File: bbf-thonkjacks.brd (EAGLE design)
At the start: 20.3 x 52.1 mm, 7 parts, among them J1 WQP-PJ301M-12_JACK, J2 WQP-PJ301M-12_JACK, J3 WQP-PJ301M-12_JACK, J4 WQP-PJ301M-12_JACK

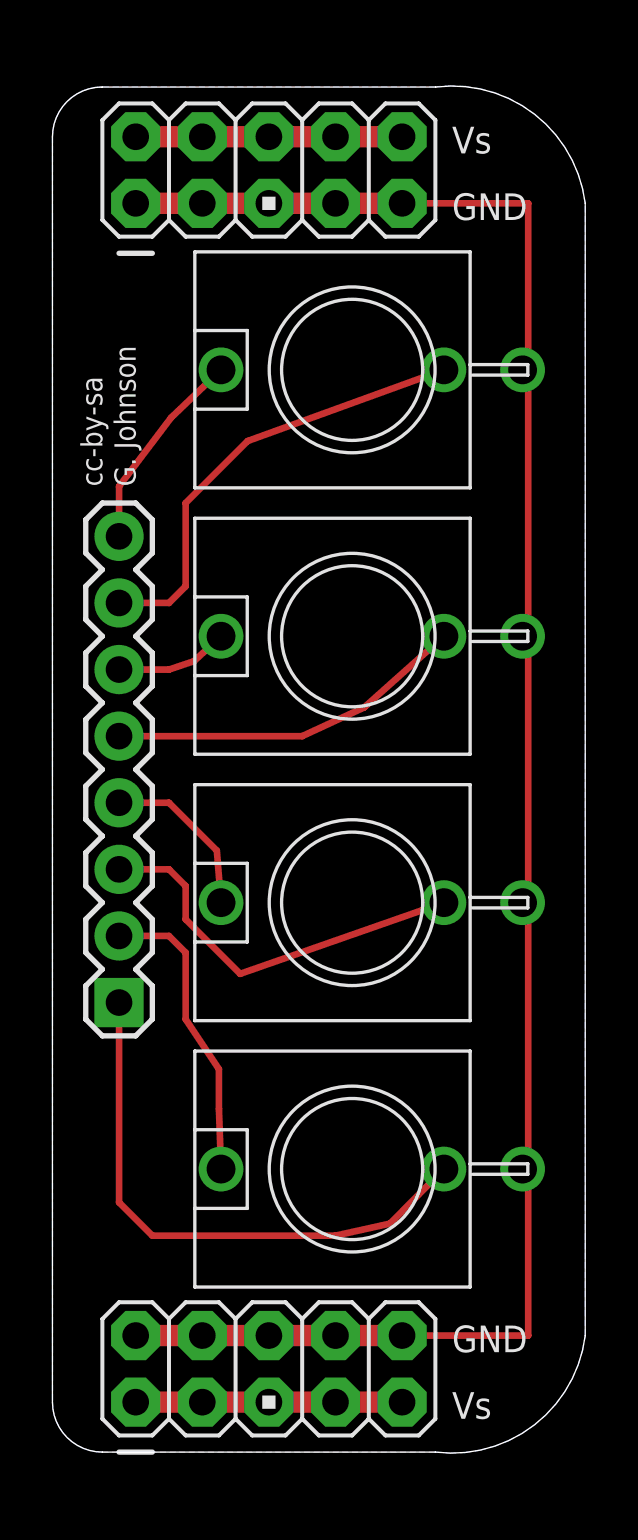
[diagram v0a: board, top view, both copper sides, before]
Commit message: thonkiconn jacks wider
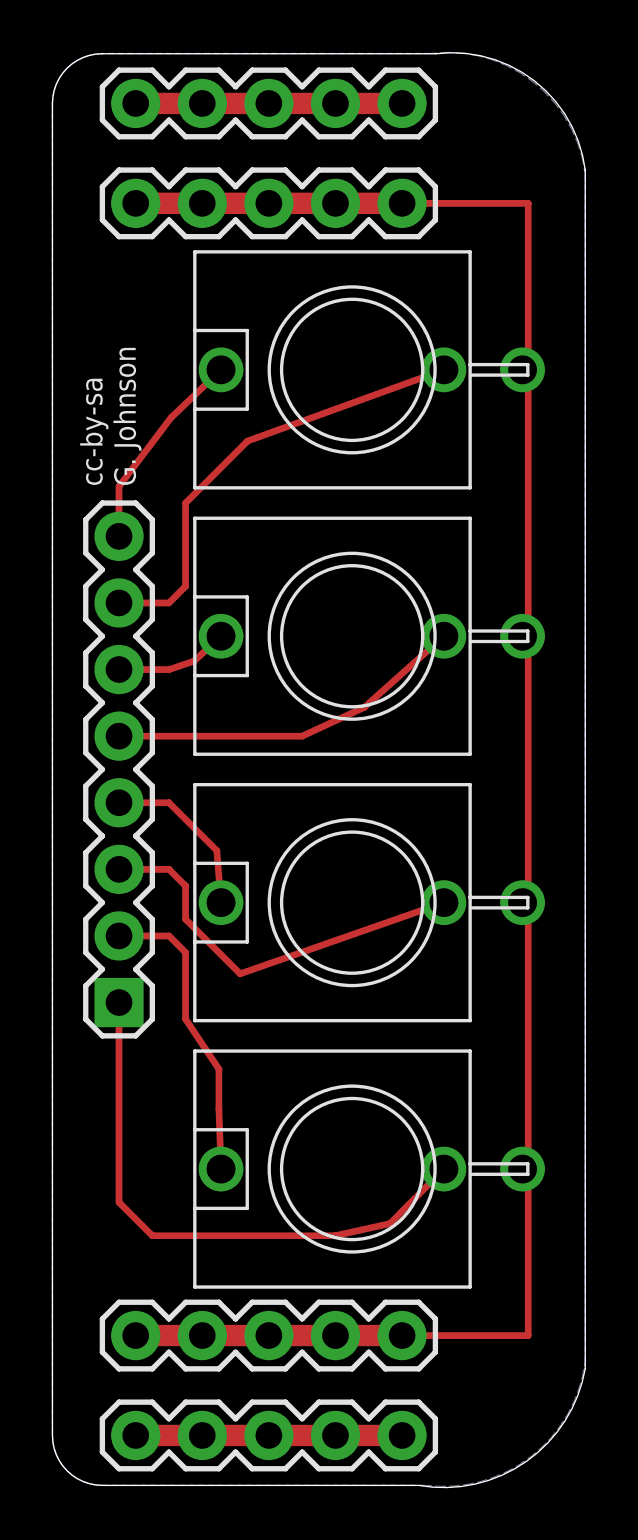
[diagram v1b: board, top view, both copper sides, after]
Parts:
- removed JP1, JP3: M05X2PTH, SparkFun:AVR_ICSP
- added JP4, JP5, JP6, JP7: (no value), SparkFun:1X05
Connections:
- net GND: now also JP4.1, JP4.2, JP4.3, JP4.4, JP4.5, JP6.1, JP6.2, JP6.3, JP6.4, JP6.5; no longer JP1.1, JP1.3, JP1.5, JP1.7, JP1.9, JP3.10, JP3.2, JP3.4, JP3.6, JP3.8
- net VCC: now also JP5.1, JP5.2, JP5.3, JP5.4, JP5.5; no longer JP1.10, JP1.2, JP1.4, JP1.6, JP1.8
- net VEE: now also JP7.1, JP7.2, JP7.3, JP7.4, JP7.5; no longer JP3.1, JP3.3, JP3.5, JP3.7, JP3.9
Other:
- board size 20.3 x 52.1 mm -> 20.3 x 54.7 mm
- board text removed: "GND"
- board text removed: "Vs"
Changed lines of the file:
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@@
 <?xml version="1.0" encoding="utf-8"?>
 <!DOCTYPE eagle SYSTEM "eagle.dtd">
-<eagle version="7.3.0">
+<eagle version="9.6.2">
 <drawing>
 <settings>
-<setting alwaysvectorfont="yes"/>
+<setting alwaysvectorfont="no"/>
+<setting keepoldvectorfont="yes"/>
 <setting verticaltext="up"/>
 </settings>
-<grid distance="25" unitdist="mil" unit="mm" style="lines" multiple="2" display="yes" altdistance="1" altunitdist="mm" altunit="mm"/>
+<grid distance="25" unitdist="mil" unit="inch" style="lines" multiple="1" display="yes" altdistance="0.025" altunitdist="inch" altunit="inch"/>
 <layers>
 <layer number="1" name="Top" color="4" fill="1" visible="yes" active="yes"/>
@@
 <board>
 <plain>
-<wire x1="14.605" y1="0" x2="20.32" y2="4.445" width="0" layer="20" curve="90"/>
-<wire x1="20.32" y1="4.445" x2="20.32" y2="47.625" width="0" layer="20"/>
-<wire x1="20.32" y1="47.625" x2="14.615" y2="52.06" width="0" layer="20" curve="90"/>
-<wire x1="14.615" y1="52.06" x2="1.895" y2="52.06" width="0" layer="20"/>
-<wire x1="1.895" y1="52.06" x2="0" y2="50.165" width="0" layer="20" curve="90"/>
-<wire x1="0" y1="50.165" x2="0" y2="1.905" width="0" layer="20"/>
-<wire x1="0" y1="1.905" x2="1.905" y2="0" width="0" layer="20" curve="90"/>
-<wire x1="1.905" y1="0" x2="14.605" y2="0" width="0" layer="20"/>
+<wire x1="13.97" y1="-1.27" x2="20.32" y2="3.175" width="0" layer="20" curve="90"/>
+<wire x1="20.32" y1="3.175" x2="20.32" y2="48.895" width="0" layer="20"/>
+<wire x1="20.32" y1="48.895" x2="14.615" y2="53.33" width="0" layer="20" curve="90"/>
+<wire x1="14.615" y1="53.33" x2="1.895" y2="53.33" width="0" layer="20"/>
+<wire x1="1.895" y1="53.33" x2="0" y2="51.435" width="0" layer="20" curve="90"/>
+<wire x1="0" y1="51.435" x2="0" y2="0.635" width="0" layer="20"/>
+<wire x1="0" y1="0.635" x2="1.905" y2="-1.27" width="0" layer="20" curve="90"/>
+<wire x1="1.905" y1="-1.27" x2="13.97" y2="-1.27" width="0" layer="20"/>
 <text x="1.905" y="36.83" size="0.8128" layer="25" ratio="15" rot="R90">cc-by-sa</text>
 <text x="3.175" y="36.83" size="0.8128" layer="25" ratio="15" rot="R90">G. Johnson</text>
-<text x="15.24" y="46.99" size="1.016" layer="21" font="vector">GND</text>
-<text x="15.24" y="3.81" size="1.016" layer="21" font="vector">GND</text>
-<text x="15.24" y="1.27" size="1.016" layer="21" font="vector">Vs</text>
-<text x="15.24" y="49.53" size="1.016" layer="21" font="vector">Vs</text>
 </plain>
 <attributes>
@@
 <param name="dpMaxLengthDifference" value="10mm"/>
 <param name="dpGapFactor" value="2.5"/>
-<param name="checkGrid" value="0"/>
 <param name="checkAngle" value="1"/>
 <param name="checkFont" value="1"/>
 <param name="checkRestrict" value="1"/>
+<param name="checkStop" value="0"/>
+<param name="checkValues" value="0"/>
+<param name="checkNames" value="1"/>
+<param name="checkWireStubs" value="1"/>
+<param name="checkPolygonWidth" value="0"/>
 <param name="useDiameter" value="13"/>
 <param name="maxErrors" value="50"/>
@@
 </autorouter>
 <elements>
-<element name="JP1" library="SparkFun" package="AVR_ICSP" value="M05X2PTH" x="8.255" y="48.895" smashed="yes" rot="R90"/>
-<element name="JP3" library="SparkFun" package="AVR_ICSP" value="M05X2PTH" x="8.255" y="3.175" smashed="yes" rot="R90"/>
 <element name="J2" library="thonkiconn" package="WQP-PJ301M-12_JACK" value="WQP-PJ301M-12_JACK" x="11.43" y="31.115" smashed="yes" rot="R90"/>
 <element name="J3" library="thonkiconn" package="WQP-PJ301M-12_JACK" value="WQP-PJ301M-12_JACK" x="11.43" y="20.955" smashed="yes" rot="R90"/>
@@
 <attribute name="VALUE" x="5.715" y="15.875" size="1.27" layer="27" rot="R90"/>
 </element>
+<element name="JP4" library="SparkFun" package="1X05" value="" x="3.175" y="47.625" smashed="yes">
+<attribute name="VALUE" x="1.905" y="44.45" size="1.27" layer="27"/>
+</element>
+<element name="JP5" library="SparkFun" package="1X05" value="" x="3.175" y="51.435" smashed="yes">
+<attribute name="VALUE" x="1.905" y="48.26" size="1.27" layer="27"/>
+</element>
+<element name="JP6" library="SparkFun" package="1X05" value="" x="3.175" y="4.445" smashed="yes">
+<attribute name="VALUE" x="1.905" y="1.27" size="1.27" layer="27"/>
+</element>
+<element name="JP7" library="SparkFun" package="1X05" value="" x="3.175" y="0.635" smashed="yes">
+<attribute name="VALUE" x="1.905" y="-2.54" size="1.27" layer="27"/>
+</element>
 </elements>
 <signals>
 <signal name="GND">
-<contactref element="JP1" pad="7"/>
-<contactref element="JP1" pad="5"/>
-<contactref element="JP1" pad="3"/>
-<contactref element="JP1" pad="1"/>
-<contactref element="JP3" pad="8"/>
-<contactref element="JP3" pad="6"/>
-<contactref element="JP3" pad="4"/>
-<contactref element="JP3" pad="2"/>
-<contactref element="JP1" pad="9"/>
-<contactref element="JP3" pad="10"/>
 <contactref element="J2" pad="P$3"/>
 <contactref element="J3" pad="P$3"/>
@@
 <contactref element="J1" pad="P$3"/>
 <polygon width="0.254" layer="16">
-<vertex x="14.605" y="0" curve="90"/>
-<vertex x="20.32" y="4.445"/>
-<vertex x="20.32" y="47.625" curve="90"/>
-<vertex x="14.605" y="52.07"/>
-<vertex x="1.905" y="52.07" curve="90"/>
-<vertex x="0" y="50.165"/>
-<vertex x="0" y="1.905" curve="90"/>
-<vertex x="1.905" y="0"/>
+<vertex x="14.24214375" y="-1.27" curve="90"/>
+<vertex x="20.32" y="3.457221875"/>
+<vertex x="20.32" y="48.7538875" curve="90"/>
+<vertex x="14.423571875" y="53.34"/>
+<vertex x="1.905" y="53.34" curve="90"/>
+<vertex x="0" y="51.435"/>
+<vertex x="0" y="0.635" curve="90"/>
+<vertex x="1.905" y="-1.27"/>
 </polygon>
 <wire x1="13.335" y1="47.625" x2="18.145" y2="47.625" width="0.254" layer="1"/>
@@
 <wire x1="3.175" y1="47.625" x2="13.335" y2="47.625" width="0.8128" layer="1"/>
 <wire x1="3.175" y1="4.445" x2="13.335" y2="4.445" width="0.8128" layer="1"/>
+<contactref element="JP4" pad="1"/>
+<contactref element="JP4" pad="5"/>
+<contactref element="JP4" pad="4"/>
+<contactref element="JP4" pad="3"/>
+<contactref element="JP4" pad="2"/>
+<contactref element="JP6" pad="5"/>
+<contactref element="JP6" pad="1"/>
+<contactref element="JP6" pad="2"/>
+<contactref element="JP6" pad="3"/>
+<contactref element="JP6" pad="4"/>
+<wire x1="13.335" y1="47.625" x2="17.93" y2="41.275" width="0" layer="19" extent="1-1"/>
+<wire x1="10.795" y1="47.625" x2="13.335" y2="47.625" width="0" layer="19" extent="1-1"/>
+<wire x1="8.255" y1="47.625" x2="10.795" y2="47.625" width="0" layer="19" extent="1-1"/>
+<wire x1="5.715" y1="47.625" x2="3.175" y2="47.625" width="0" layer="19" extent="1-1"/>
+<wire x1="10.795" y1="4.445" x2="13.335" y2="4.445" width="0" layer="19" extent="1-1"/>
+<wire x1="8.255" y1="4.445" x2="10.795" y2="4.445" width="0" layer="19" extent="1-1"/>
+<wire x1="5.715" y1="4.445" x2="3.175" y2="4.445" width="0" layer="19" extent="1-1"/>
+<wire x1="17.93" y1="10.795" x2="13.335" y2="4.445" width="0" layer="19" extent="1-1"/>
+<wire x1="17.93" y1="31.115" x2="17.93" y2="41.275" width="0" layer="19" extent="1-1"/>
+<wire x1="17.93" y1="20.955" x2="17.93" y2="10.795" width="0" layer="19" extent="1-1"/>
 </signal>
 <signal name="VCC">
-<contactref element="JP1" pad="8"/>
-<contactref element="JP1" pad="6"/>
-<contactref element="JP1" pad="4"/>
-<contactref element="JP1" pad="2"/>
-<contactref element="JP1" pad="10"/>
-<wire x1="3.175" y1="50.165" x2="5.715" y2="50.165" width="0.8128" layer="1"/>
-<wire x1="5.715" y1="50.165" x2="8.255" y2="50.165" width="0.8128" layer="1"/>
-<wire x1="8.255" y1="50.165" x2="10.795" y2="50.165" width="0.8128" layer="1"/>
-<wire x1="10.795" y1="50.165" x2="13.335" y2="50.165" width="0.8128" layer="1"/>
+<contactref element="JP5" pad="5"/>
+<contactref element="JP5" pad="1"/>
+<contactref element="JP5" pad="2"/>
+<contactref element="JP5" pad="3"/>
+<contactref element="JP5" pad="4"/>
+<wire x1="3.175" y1="51.435" x2="5.715" y2="51.435" width="0.8128" layer="1"/>
+<wire x1="5.715" y1="51.435" x2="8.255" y2="51.435" width="0.8128" layer="1"/>
+<wire x1="8.255" y1="51.435" x2="10.795" y2="51.435" width="0.8128" layer="1"/>
+<wire x1="10.795" y1="51.435" x2="13.335" y2="51.435" width="0.8128" layer="1"/>
 </signal>
 <signal name="VEE">
-<contactref element="JP3" pad="7"/>
-<contactref element="JP3" pad="5"/>
-<contactref element="JP3" pad="3"/>
-<contactref element="JP3" pad="1"/>
-<contactref element="JP3" pad="9"/>
-<wire x1="3.175" y1="1.905" x2="5.715" y2="1.905" width="0.8128" layer="1"/>
-<wire x1="5.715" y1="1.905" x2="8.255" y2="1.905" width="0.8128" layer="1"/>
-<wire x1="8.255" y1="1.905" x2="10.795" y2="1.905" width="0.8128" layer="1"/>
-<wire x1="10.795" y1="1.905" x2="13.335" y2="1.905" width="0.8128" layer="1"/>
+<contactref element="JP7" pad="1"/>
+<contactref element="JP7" pad="5"/>
+<contactref element="JP7" pad="4"/>
+<contactref element="JP7" pad="3"/>
+<contactref element="JP7" pad="2"/>
+<wire x1="3.175" y1="0.635" x2="5.715" y2="0.635" width="0.8128" layer="1"/>
+<wire x1="5.715" y1="0.635" x2="8.255" y2="0.635" width="0.8128" layer="1"/>
+<wire x1="8.255" y1="0.635" x2="10.795" y2="0.635" width="0.8128" layer="1"/>
+<wire x1="10.795" y1="0.635" x2="13.335" y2="0.635" width="0.8128" layer="1"/>
 </signal>
 <signal name="N$1">
@@
 </signal>
 </signals>
+<mfgpreviewcolors>
+<mfgpreviewcolor name="soldermaskcolor" color="0xC8008000"/>
+<mfgpreviewcolor name="silkscreencolor" color="0xFFFEFEFE"/>
+<mfgpreviewcolor name="backgroundcolor" color="0xFF282828"/>
+<mfgpreviewcolor name="coppercolor" color="0xFFFFBF00"/>
+<mfgpreviewcolor name="substratecolor" color="0xFF786E46"/>
+</mfgpreviewcolors>
 </board>
 </drawing>
